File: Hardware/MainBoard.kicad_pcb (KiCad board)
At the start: 2 copper layers, 100 x 40 mm, 39 parts, among them J1 UPDI, J2 UART, J3 DCF77, J4 Vin, J5 HVReg, U1 HV5623K7-G, U2 HV5623K7-G, U3 ATtiny1606-S, U4 L78L05_SOT89, U5 DS3231MZ

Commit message: Start rework
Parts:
- removed C4: 100n, Capacitor_SMD:C_0603_1608Metric_Pad1.05x0.95mm_HandSolder
- removed C5: 10n, Capacitor_SMD:C_0603_1608Metric_Pad1.05x0.95mm_HandSolder
- removed J5: HVReg, Nixies:NCH8200HV
- removed R8: 4k7, Resistor_SMD:R_0603_1608Metric_Pad1.05x0.95mm_HandSolder
- removed R9: 10k, Resistor_SMD:R_0603_1608Metric_Pad1.05x0.95mm_HandSolder
- removed U5: DS3231MZ, Package_SO:SOIC-8_3.9x4.9mm_P1.27mm
- added REG1: HVReg, Nixies:NCH8200HV, F.Cu at (70.0, 51.9)
- J2: footprint Connector_PinHeader_2.54mm:PinHeader_1x03_P2.54mm_Vertical -> Connector_PinHeader_2.54mm:PinHeader_1x02_P2.54mm_Vertical
- J3: value DCF77 -> NMEA; footprint DCF77:ELV_DCF-2_91610 -> Connector_PinHeader_1.00mm:PinHeader_1x06_P1.00mm_Vertical
- N1, N2, N3, N4: footprint Nixies:nixies-us-IN-14 -> Nixies:IN-14
- R6: value 10k -> 100k
- R7: value 4k7 -> 100k
- U1, U2: value HV5623K7-G -> HV5530; footprint hv5623:HV5623K7-G -> Package_QFP:PQFP-44_10x10mm_P0.8mm
- moved R5 153.8 mm to (-70.8, 80.8), turned to 0 degrees
- moved R4 146.2 mm to (-32.7, 68.6), turned to 0 degrees
- moved C3 142.9 mm to (-75.2, 79.7)
- moved J1 133.5 mm to (-47.2, 58.4), turned to 0 degrees
- moved C2 129.2 mm to (-27.6, 68.2), turned to 0 degrees
- moved R3 117.5 mm to (-26.8, 62.0), turned to 0 degrees
- moved J2 97.3 mm to (-47.2, 77.0), turned to 0 degrees
- moved R2 87.0 mm to (-32.7, 65.3), turned to 0 degrees
- moved R1 65.0 mm to (-32.7, 62.0), turned to 0 degrees
- moved C1 62.9 mm to (-21.6, 61.6), turned to 0 degrees
- moved J4 57.1 mm to (82.3, 56.9)
- moved U3 51.6 mm to (51.8, 101.1), turned to 90 degrees
- moved J3 43.4 mm to (102.8, 69.2)
- moved R6 38.5 mm to (90.5, 63.8), turned to 0 degrees
- moved F2 38.4 mm to (71.6, 52.8), turned to 180 degrees
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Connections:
- J2 pad 1: UART_RxD -> UART_TxD
- J2 pad 2: UART_TxD -> GND
- J3 pad 1: +5V -> Net-(J3-Pad1)
- J3 pad 2: DCF77 -> +5V
- J3 pad 3: GND -> Net-(J3-Pad3)
- N1 pad LHDP: /NixieTubes/N1_R -> /NixieTubes/N1_L
- N1 pad RHDP: /NixieTubes/N1_L -> /NixieTubes/N1_R
- N2 pad LHDP: /NixieTubes/N2_R -> /NixieTubes/N2_L
- N2 pad RHDP: /NixieTubes/N2_L -> /NixieTubes/N2_R
- N3 pad LHDP: /NixieTubes/N3_R -> /NixieTubes/N3_L
- N3 pad RHDP: /NixieTubes/N3_L -> /NixieTubes/N3_R
- N4 pad LHDP: /NixieTubes/N4_R -> /NixieTubes/N4_L
- N4 pad RHDP: /NixieTubes/N4_L -> /NixieTubes/N4_R
- R6 pad 2: DCF77 -> NMEA_RxD
- R7 pad 2: RTC_SDA -> Net-(J3-Pad3)
- U3 pad 10: RTC_SDA -> Net-(U3-Pad10)
- U3 pad 11: RTC_SCL -> Net-(U3-Pad11)
- U3 pad 14: DCF77 -> NMEA_SYNC
- U3 pad 18: RTC_SQW -> Net-(U3-Pad18)
- U3 pad 8: UART_RxD -> NMEA_RxD
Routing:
- net +5V: track 207.1 -> 5.08 mm, vias 8 -> 0
- net 170V: track 151.1 -> 62.3 mm
- net Net-(U1-Pad23): track 77.2 -> 0.00 mm
- net NIX_DIM: track 74.7 -> 0.00 mm, vias 4 -> 0
- net NIX_CLK: track 74.4 -> 0.00 mm, vias 6 -> 0
- net NIX_LE: track 73.3 -> 0.00 mm, vias 2 -> 0
- net DCF77: track 70.7 -> 0.00 mm, vias 4 -> 0
- net +12V: track 39.5 -> 0.00 mm
- net /NixieTubes/N_DOT: track 32.1 -> 0.00 mm
- net /NixieTubes/N2_7: track 26.2 -> 0.00 mm
- net /NixieTubes/N4_7: track 26.2 -> 0.00 mm
- net /NixieTubes/N3_4: track 26.2 -> 0.00 mm
- net /NixieTubes/N1_4: track 26.2 -> 0.00 mm
- net /NixieTubes/N4_8: track 24.5 -> 0.00 mm
- net /NixieTubes/N3_3: track 24.5 -> 0.00 mm
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- removed copper zone on B.Cu, net +5V
- removed copper zone on F.Cu, net +5V
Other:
- board text removed: "12V"
- board text removed: "5V"
- board text removed: "DCF"
- board text removed: "GND"
- board text removed: "HV"
- board text removed: "RxD"
- board text removed: "TxD"
- board text removed: "UPDI"

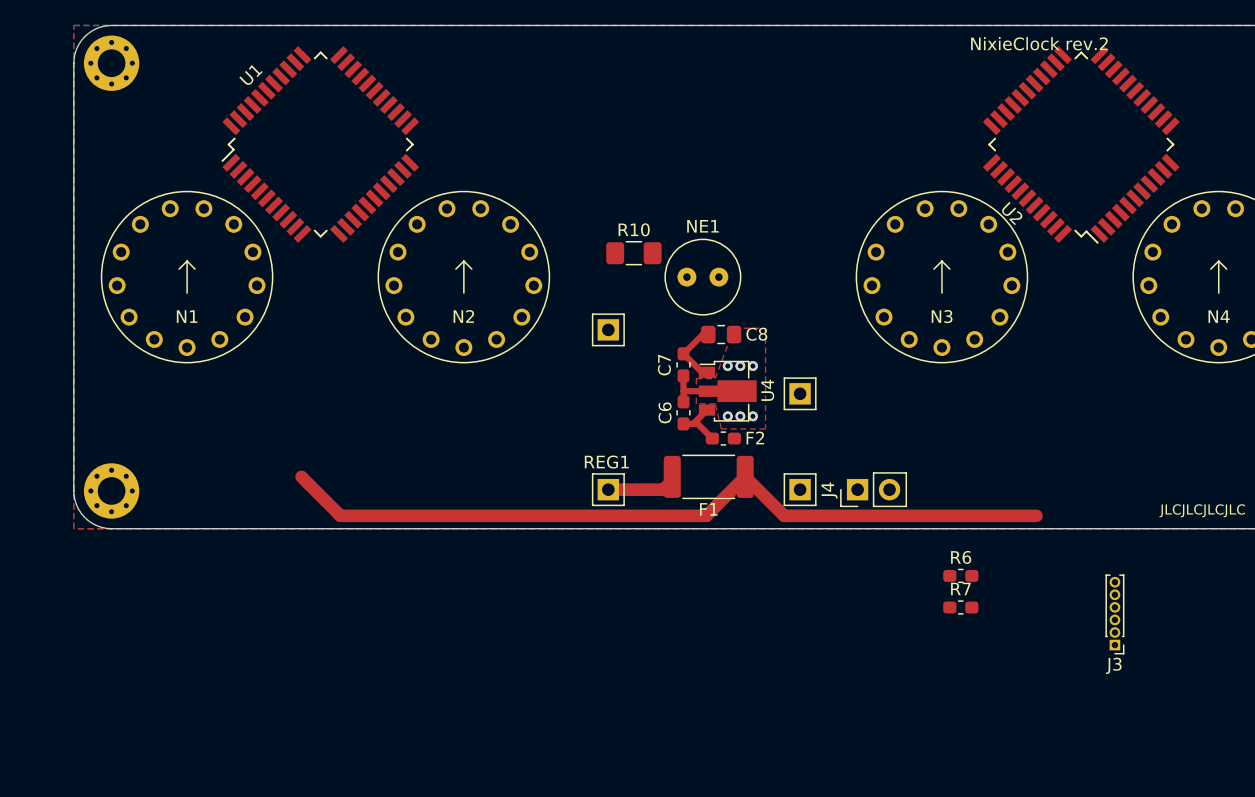
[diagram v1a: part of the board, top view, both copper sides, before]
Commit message: Fix packages, route left nixies
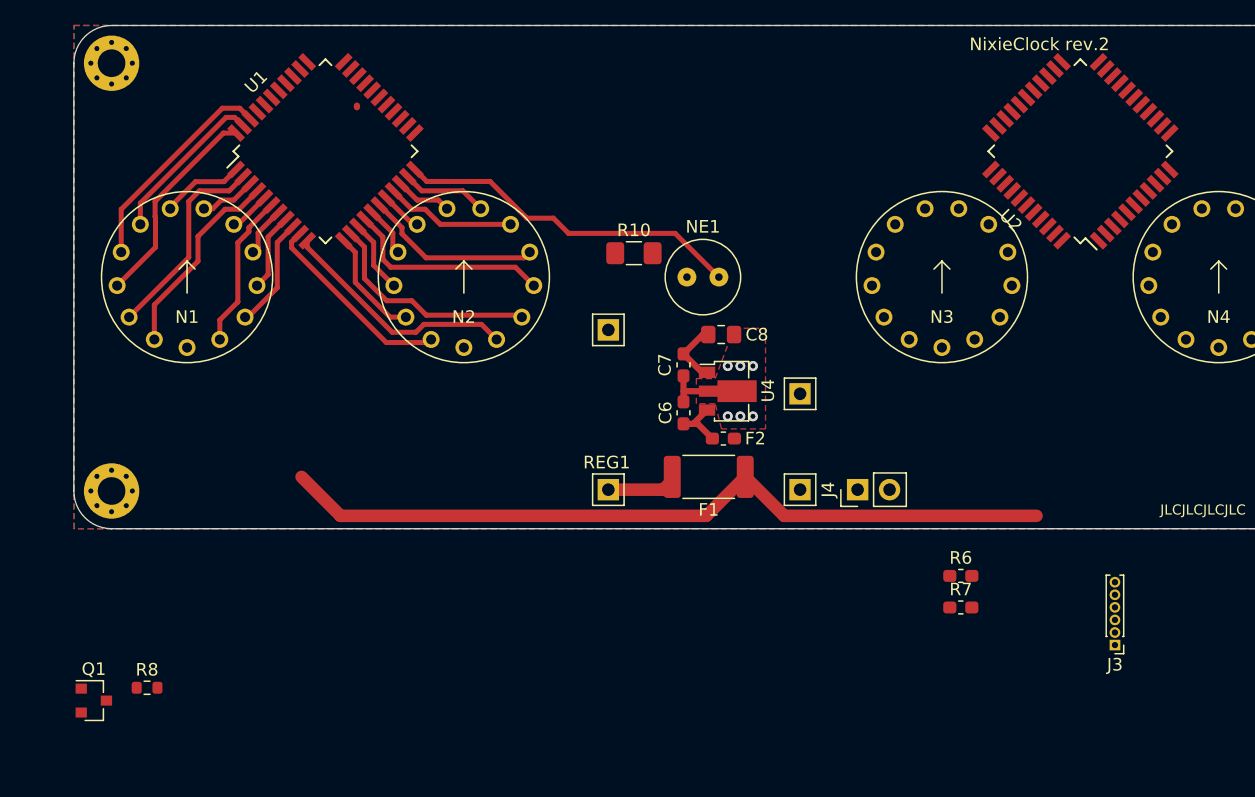
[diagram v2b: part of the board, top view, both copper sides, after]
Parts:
- added Q1: S8050, Package_TO_SOT_SMD:SOT-23, F.Cu at (21.6, 73.7)
- added R8: 10k, Resistor_SMD:R_0603_1608Metric, F.Cu at (25.8, 72.6)
- R6: value 100k -> 10k
- moved U1 0.65 mm to (40.0, 30.0)
- moved U2 0.54 mm to (100.0, 30.0)
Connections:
- J3 pad 4: NMEA_RxD -> Net-(J3-Pad4)
- U1 pad 1: /NixieTubes/N2_3 -> /NixieTubes/N1_5
- U1 pad 10: /NixieTubes/N1_7 -> /NixieTubes/N2_L
- U1 pad 11: /NixieTubes/N1_8 -> /NixieTubes/N2_R
- U1 pad 12: /NixieTubes/N1_9 -> /NixieTubes/N2_1
- U1 pad 13: /NixieTubes/N1_0 -> /NixieTubes/N2_0
- U1 pad 14: /NixieTubes/N1_R -> /NixieTubes/N2_2
- U1 pad 15: /NixieTubes/N1_L -> /NixieTubes/N2_9
- U1 pad 16: /NixieTubes/N1_1 -> /NixieTubes/N2_3
- U1 pad 17: /NixieTubes/N1_2 -> /NixieTubes/N2_8
- U1 pad 18: /NixieTubes/N1_3 -> /NixieTubes/N2_4
- U1 pad 19: Net-(U1-Pad19) -> /NixieTubes/N2_7
- U1 pad 2: /NixieTubes/N2_4 -> /NixieTubes/N1_1
- U1 pad 20: Net-(U1-Pad20) -> /NixieTubes/N2_5
- U1 pad 21: Net-(U1-Pad21) -> /NixieTubes/N2_6
- U1 pad 22: Net-(U1-Pad22) -> /NixieTubes/N_DOT
- U1 pad 3: /NixieTubes/N2_5 -> /NixieTubes/N1_6
- U1 pad 37: /NixieTubes/N_DOT -> Net-(U1-Pad37)
- U1 pad 38: /NixieTubes/N2_8 -> Net-(U1-Pad38)
- U1 pad 39: /NixieTubes/N2_9 -> Net-(U1-Pad39)
- U1 pad 4: /NixieTubes/N2_6 -> /NixieTubes/N1_L
- U1 pad 40: /NixieTubes/N2_0 -> Net-(U1-Pad40)
- U1 pad 41: /NixieTubes/N2_R -> Net-(U1-Pad41)
- U1 pad 42: /NixieTubes/N2_L -> /NixieTubes/N1_3
- U1 pad 43: /NixieTubes/N2_1 -> /NixieTubes/N1_4
- U1 pad 44: /NixieTubes/N2_2 -> /NixieTubes/N1_2
- U1 pad 5: /NixieTubes/N2_7 -> /NixieTubes/N1_7
- U1 pad 6: Net-(U1-Pad6) -> /NixieTubes/N1_R
- U1 pad 7: /NixieTubes/N1_4 -> /NixieTubes/N1_8
- U1 pad 8: /NixieTubes/N1_5 -> /NixieTubes/N1_9
- U1 pad 9: /NixieTubes/N1_6 -> /NixieTubes/N1_0
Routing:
- net /NixieTubes/N_DOT: track 0.00 -> 27.7 mm
- net /NixieTubes/N2_R: track 0.00 -> 19.1 mm
- net /NixieTubes/N2_0: track 0.00 -> 17.8 mm
- net /NixieTubes/N1_3: track 0.00 -> 17.3 mm
- net /NixieTubes/N1_2: track 0.00 -> 16.7 mm
- net /NixieTubes/N2_9: track 0.00 -> 16.6 mm
- net /NixieTubes/N1_1: track 0.00 -> 16.3 mm
- net /NixieTubes/N1_L: track 0.00 -> 15.9 mm
- net /NixieTubes/N2_L: track 0.00 -> 15.7 mm
- net /NixieTubes/N2_8: track 0.00 -> 14.2 mm
- net /NixieTubes/N1_4: track 0.00 -> 13.0 mm
- net /NixieTubes/N1_R: track 0.00 -> 12.4 mm
- net /NixieTubes/N2_7: track 0.00 -> 10.4 mm
- net /NixieTubes/N1_0: track 0.00 -> 8.92 mm
- net /NixieTubes/N2_1: track 0.00 -> 8.86 mm
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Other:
- net class MV added: clearance 0.33, trace_width 0.25, via_dia 0.8, via_drill 0.4

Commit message: More layouting
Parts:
- J3: footprint Connector_PinHeader_1.00mm:PinHeader_1x06_P1.00mm_Vertical -> Connector_PinHeader_1.27mm:PinHeader_1x06_P1.27mm_Vertical
- moved R5 150.2 mm to (65.1, 17.0)
- moved R4 145.0 mm to (111.0, 49.5), turned to 90 degrees
- moved J2 143.8 mm to (81.5, 13.0)
- moved C3 137.1 mm to (46.5, 16.5)
- moved C2 132.2 mm to (94.5, 17.5), turned to 180 degrees
- moved J1 122.0 mm to (66.0, 13.0), turned to 270 degrees
- moved R3 116.4 mm to (89.0, 49.5), turned to 90 degrees
- moved C1 98.6 mm to (73.6, 36.0), turned to 180 degrees
- moved Q1 95.5 mm to (93.9, 11.3), turned to 180 degrees
- moved R8 93.7 mm to (96.8, 11.4), turned to 90 degrees
- moved R2 85.2 mm to (51.0, 49.5), turned to 90 degrees
- moved U3 74.8 mm to (70.0, 28.5), turned to 180 degrees
- moved R1 63.0 mm to (29.0, 49.5), turned to 90 degrees
- moved R7 53.0 mm to (85.5, 13.5)
- moved R6 52.5 mm to (90.9, 11.3), turned to 90 degrees
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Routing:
- net 170V: track 62.3 -> 112.1 mm
- net +5V: track 5.08 -> 17.2 mm
- net +12V: track 0.00 -> 4.57 mm
- net Net-(NE1-Pad2): track 0.00 -> 2.73 mm

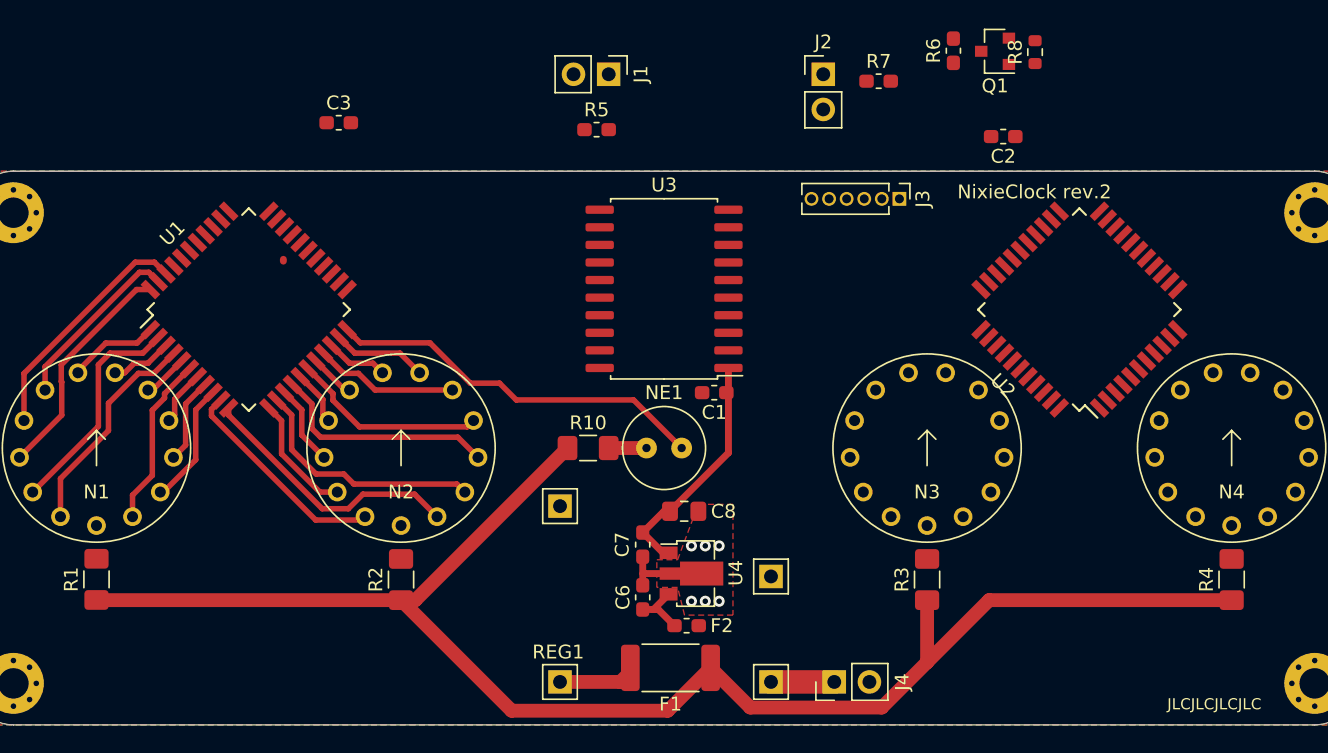
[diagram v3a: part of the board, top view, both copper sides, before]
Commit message: Replace LDO
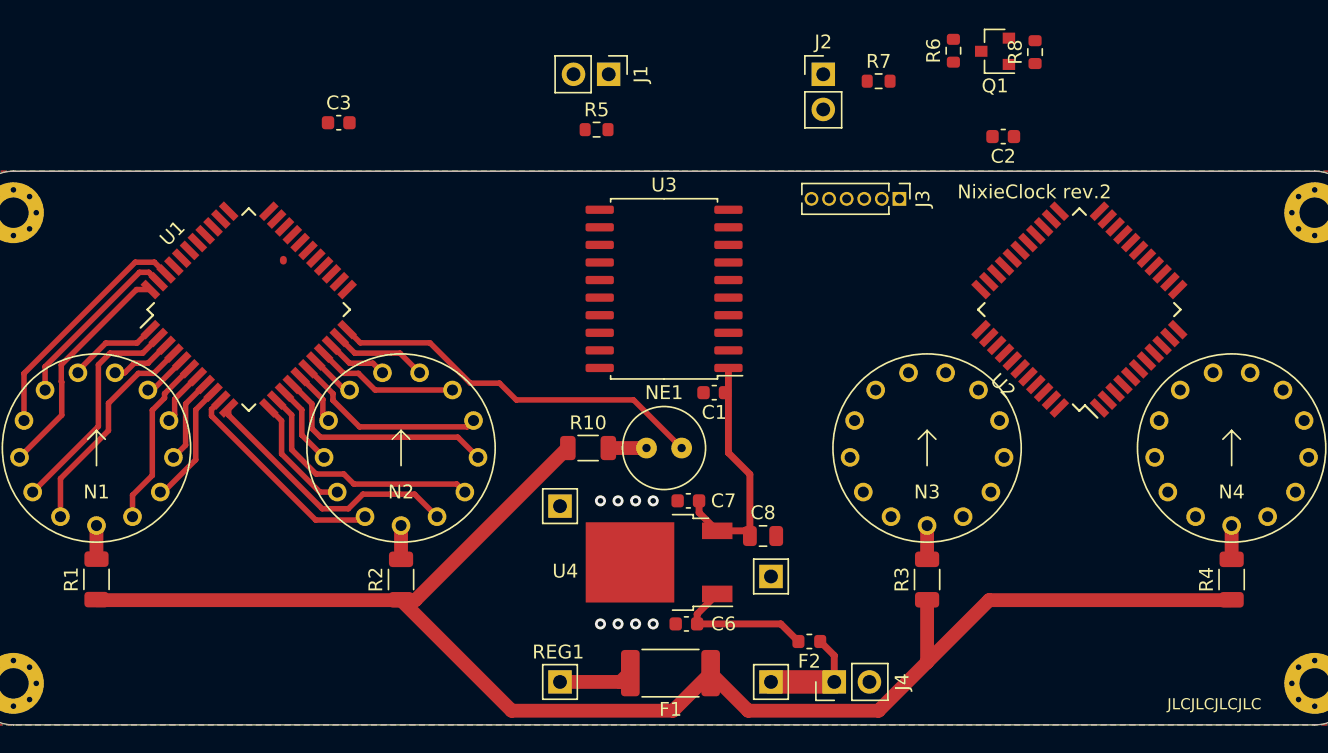
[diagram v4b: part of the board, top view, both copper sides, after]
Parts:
- C1, C2, C3, C6, C7: footprint Capacitor_SMD:C_0603_1608Metric_Pad1.05x0.95mm_HandSolder -> Capacitor_SMD:C_0603_1608Metric
- C8: footprint Capacitor_SMD:C_0805_2012Metric_Pad1.15x1.40mm_HandSolder -> Capacitor_SMD:C_0805_2012Metric
- F2: footprint Fuse:Fuse_0603_1608Metric_Pad1.05x0.95mm_HandSolder -> Fuse:Fuse_0603_1608Metric
- R1, R10, R2, R3, R4: footprint Resistor_SMD:R_1206_3216Metric_Pad1.42x1.75mm_HandSolder -> Resistor_SMD:R_1206_3216Metric
- R5, R6, R7: footprint Resistor_SMD:R_0603_1608Metric_Pad1.05x0.95mm_HandSolder -> Resistor_SMD:R_0603_1608Metric
- U4: value L78L05_SOT89 -> L78M05ABDT-TR; footprint Package_TO_SOT_SMD:SOT-89-3 -> Package_TO_SOT_SMD:TO-252-2
- moved F2 8.94 mm to (80.5, 54.0)
- moved C8 5.97 mm to (77.2, 46.4)
- moved C7 4.57 mm to (71.8, 43.8), turned to 180 degrees
- moved C6 3.69 mm to (71.6, 52.7), turned to 180 degrees
- moved U4 2.47 mm to (69.6, 48.3), turned to 180 degrees
- moved F1 0.38 mm to (70.5, 56.3)
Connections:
- U4 pad 1: +5V -> Net-(C6-Pad1)
- U4 pad 3: Net-(C6-Pad1) -> +5V
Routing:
- net Net-(C6-Pad1): track 4.68 -> 10.6 mm
- net GND: track 4.13 -> 0.13 mm, vias 6 -> 8
- net +12V: track 4.57 -> 7.91 mm
- net Net-(N4-PadA): track 0.00 -> 2.44 mm
- net Net-(N3-PadA): track 0.00 -> 2.44 mm
- net Net-(N2-PadA): track 0.00 -> 2.44 mm
- net Net-(N1-PadA): track 0.00 -> 2.42 mm
- net +5V: track 17.2 -> 18.0 mm

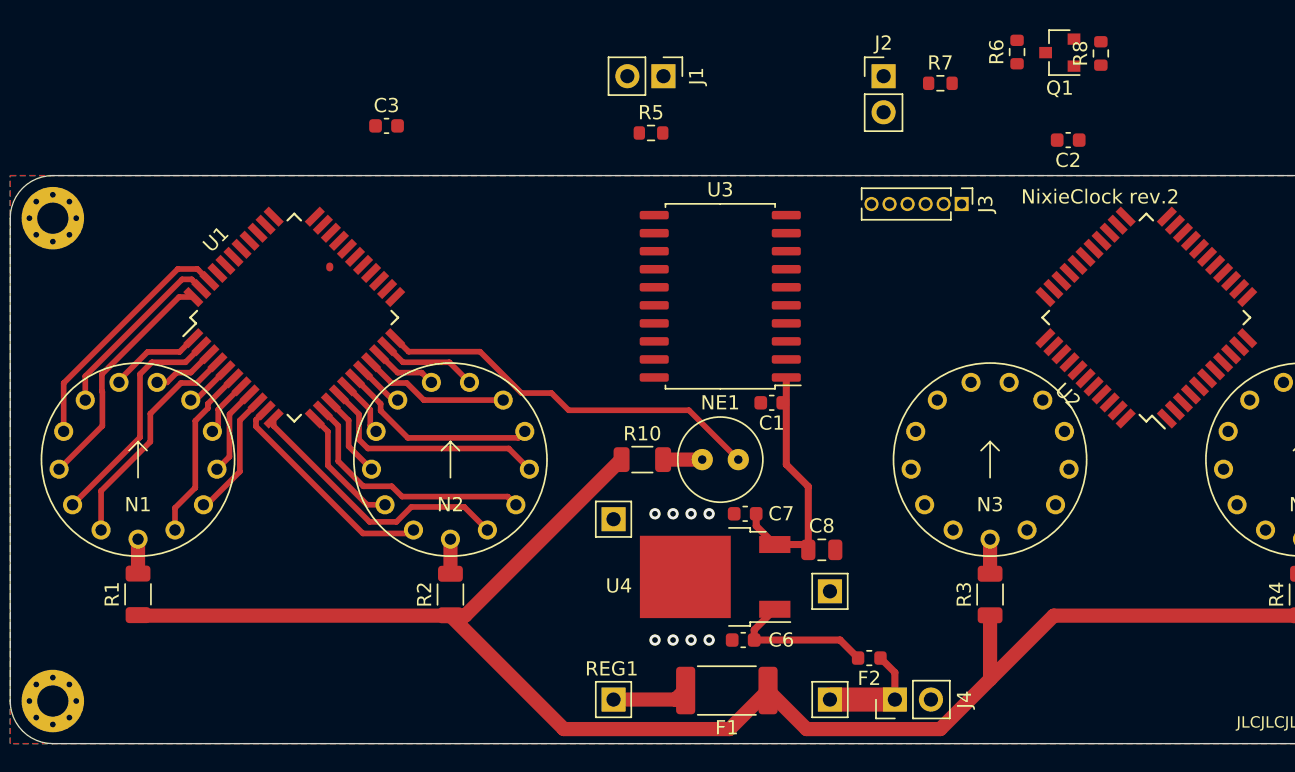
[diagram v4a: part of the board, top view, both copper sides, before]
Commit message: Route UPDI and UART
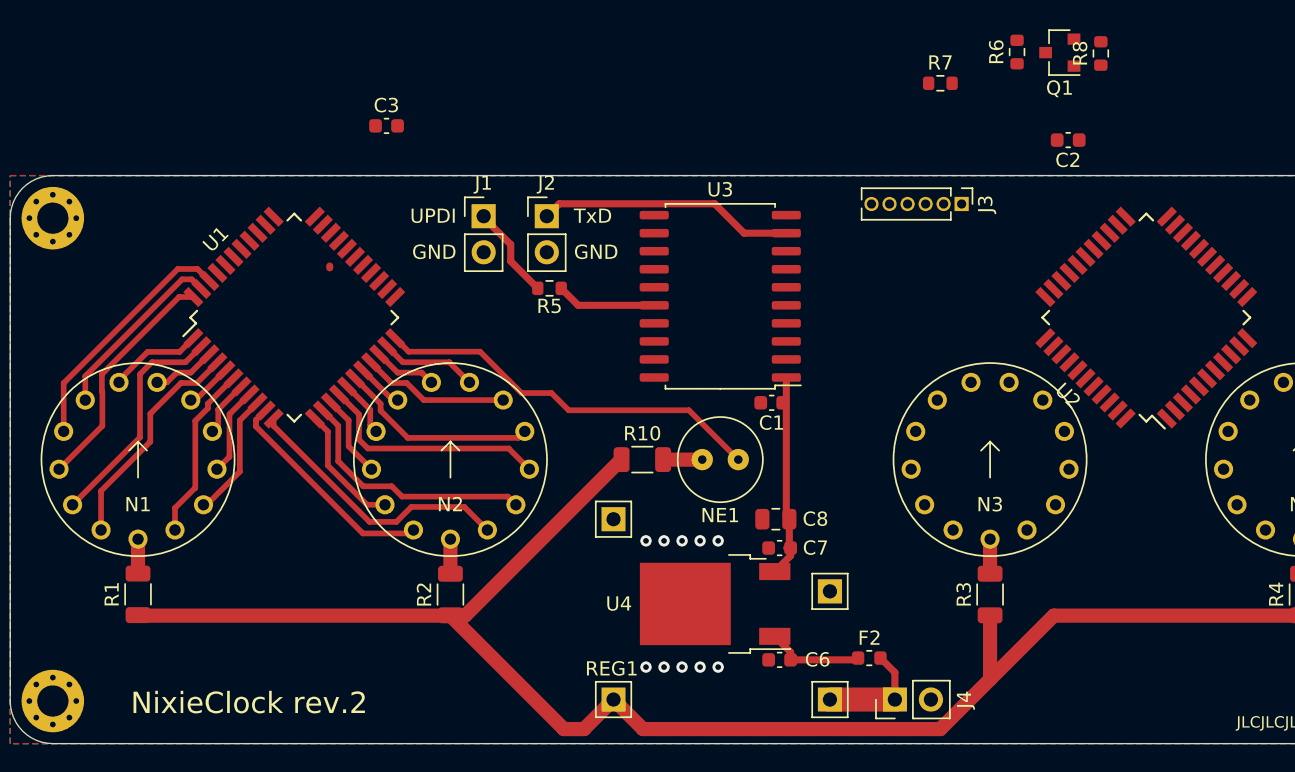
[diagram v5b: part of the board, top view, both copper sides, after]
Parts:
- removed F1: 200mA, Fuse:Fuse_2512_6332Metric
- moved J2 25.7 mm to (57.8, 22.9)
- moved J1 16.0 mm to (53.3, 22.9), turned to 0 degrees
- moved R5 13.1 mm to (58.0, 27.9)
- moved C8 3.89 mm to (73.9, 44.2), turned to 180 degrees
- moved C7 3.42 mm to (74.2, 46.2)
- moved C6 2.92 mm to (74.2, 54.1)
- moved U4 1.91 mm to (69.6, 50.2)
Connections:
- REG1 pad 2: Net-(F1-Pad2) -> 170V
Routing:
- net UART_TxD: track 0.00 -> 18.1 mm
- net UPDI: track 0.00 -> 7.04 mm
- net Net-(J1-Pad1): track 0.00 -> 6.66 mm
- net Net-(F1-Pad2): track 5.08 -> 0.00 mm
- net +5V: track 18.0 -> 14.3 mm
- net Net-(C6-Pad1): track 10.6 -> 6.92 mm
- net 170V: track 111.9 -> 111.4 mm
- net GND: vias 8 -> 10
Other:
- board text added: "GND"
- board text added: "TxD"
- board text added: "UPDI"
